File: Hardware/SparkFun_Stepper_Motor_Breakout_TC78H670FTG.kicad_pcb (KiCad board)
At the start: 4 copper layers, 15.2 x 20.3 mm, 45 parts, among them J1 Conn_01x08, J2 Conn_01x08, U1 TC78H670FTG

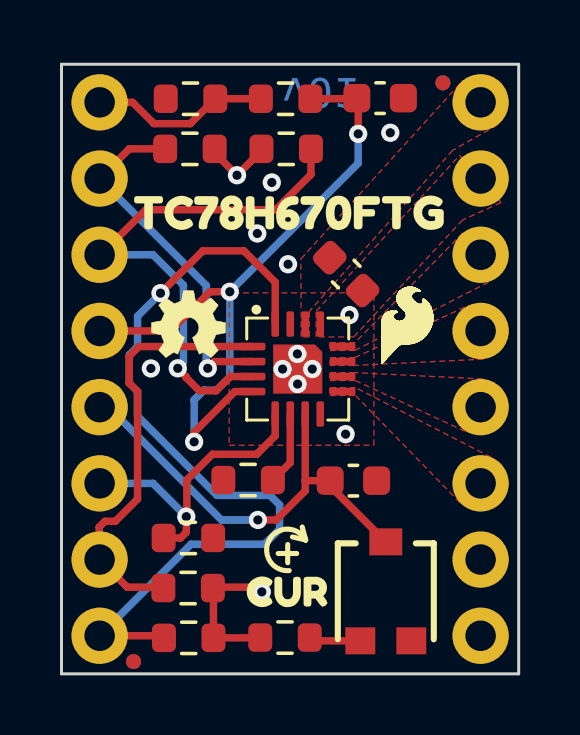
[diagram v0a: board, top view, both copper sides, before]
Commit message: moved fiducials inward
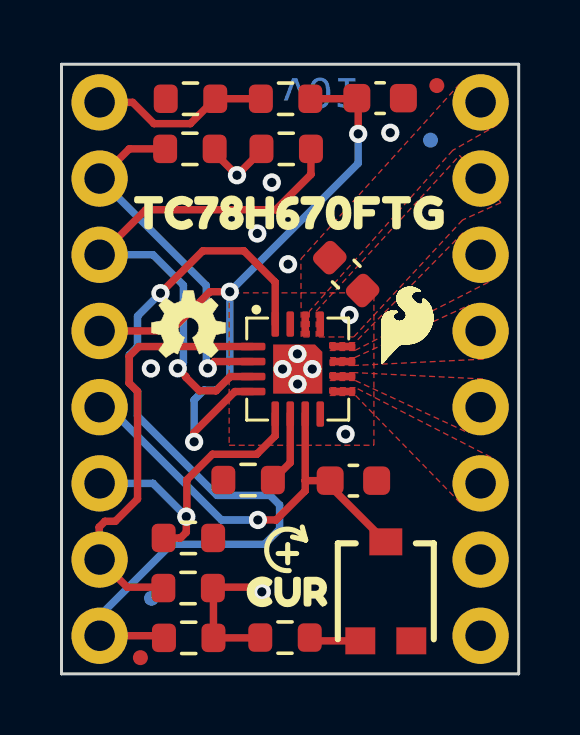
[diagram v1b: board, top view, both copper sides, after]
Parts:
- moved FID3 2.19 mm to (137.6, 111.8)
- moved FID2 1.95 mm to (146.9, 96.5)
- moved FID4 0.26 mm to (137.2, 113.8)
- moved FID1 0.22 mm to (147.1, 94.7)
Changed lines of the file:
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@@
   )
   (footprint "SparkFun-Aesthetic:Fiducial_0.5mm_Mask1mm" (layer "F.Cu")
-    (at 137.021639 113.891825)
+    (at 137.25 113.76)
     (descr "Circular Fiducial, 0.5mm bare copper, 1mm soldermask opening (Level C)")
     (tags "fiducial")
@@
   )
   (footprint "SparkFun-Aesthetic:Fiducial_0.5mm_Mask1mm" (layer "F.Cu")
-    (at 147.331908 94.601097)
+    (at 147.13 94.69)
     (descr "Circular Fiducial, 0.5mm bare copper, 1mm soldermask opening (Level C)")
     (tags "fiducial")
@@
   )
   (footprint "SparkFun-Aesthetic:Fiducial_0.5mm_Mask1mm" (layer "B.Cu")
-    (at 147.331908 94.599043 180)
+    (at 146.92 96.51 180)
     (descr "Circular Fiducial, 0.5mm bare copper, 1mm soldermask opening (Level C)")
     (tags "fiducial")
@@
   )
   (footprint "SparkFun-Aesthetic:Fiducial_0.5mm_Mask1mm" (layer "B.Cu")
-    (at 137.019585 113.89097 180)
+    (at 137.62 111.78 180)
     (descr "Circular Fiducial, 0.5mm bare copper, 1mm soldermask opening (Level C)")
     (tags "fiducial")
@@
     (pts (xy 135.89 114.3) (xy 135.89 113.03))
     (height -5.08)
-    (gr_text "0.05 in" (at 131.953695 112.297205) (layer "Eco1.User")
+    (gr_text "1.27 mm" (at 131.953695 112.297205) (layer "Eco1.User")
       (effects (font (size 0.762 0.762) (thickness 0.15)))
     )
@@
     (pts (xy 134.62 114.3) (xy 134.62 93.98))
     (height -11.43)
-    (gr_text "0.80 in" (at 122.278 104.14 90) (layer "Eco1.User")
+    (gr_text "20.32 mm" (at 122.278 104.14 90) (layer "Eco1.User")
       (effects (font (size 0.762 0.762) (thickness 0.15)))
     )
@@
     (pts (xy 134.62 93.98) (xy 149.86 93.98))
     (height -11.43)
-    (gr_text "0.60 in" (at 142.24 81.638) (layer "Eco1.User")
+    (gr_text "15.24 mm" (at 142.24 81.638) (layer "Eco1.User")
       (effects (font (size 0.762 0.762) (thickness 0.15)))
     )
@@
     (pts (xy 135.89 114.3) (xy 135.89 110.49))
     (height -8.89)
-    (gr_text "0.15 in" (at 125.582655 111.76 90) (layer "Eco1.User")
+    (gr_text "3.81 mm" (at 125.582655 111.76 90) (layer "Eco1.User")
       (effects (font (size 0.762 0.762) (thickness 0.15)))
     )
@@
     (pts (xy 134.62 95.25) (xy 148.59 95.25))
     (height -8.89)
-    (gr_text "0.55 in" (at 141.605 85.448) (layer "Eco1.User")
+    (gr_text "13.97 mm" (at 141.605 85.448) (layer "Eco1.User")
       (effects (font (size 0.762 0.762) (thickness 0.15)))
     )
@@
     (pts (xy 134.62 95.25) (xy 135.89 95.25))
     (height -5.08)
-    (gr_text "0.05 in" (at 137.01647 88.792448) (layer "Eco1.User")
+    (gr_text "1.27 mm" (at 137.01647 88.792448) (layer "Eco1.User")
       (effects (font (size 0.762 0.762) (thickness 0.15)))
     )
@@
     (height 6.56)
     (orientation 0)
-    (gr_text "0.426 in" (at 140.025 117.198) (layer "Eco1.User")
+    (gr_text "10.810 mm" (at 140.025 117.198) (layer "Eco1.User")
       (effects (font (size 0.762 0.762) (thickness 0.15)))
     )
@@
     (height 8.24)
     (orientation 1)
-    (gr_text "0.108 in" (at 153.837301 110.772841) (layer "Eco1.User")
+    (gr_text "2.750 mm" (at 153.837301 110.772841) (layer "Eco1.User")
       (effects (font (size 0.762 0.762) (thickness 0.15)))
     )
@@
   (segment (start 135.89 113.03) (end 137.965 113.03) (width 0.25) (layer "F.Cu") (net 1))
   (via (at 137.92 101.61) (size 0.6096) (drill 0.3048) (layers "F.Cu" "B.Cu") (net 1))
-  (segment (start 137.1548 104.886102) (end 137.1548 105.7048) (width 0.25) (layer "B.Cu") (net 1))
-  (segment (start 138.94 109.98) (end 135.89 113.03) (width 0.25) (layer "B.Cu") (net 1))
-  (segment (start 141.57 108.35) (end 141.89 108.67) (width 0.25) (layer "B.Cu") (net 1))
   (segment (start 141.89 108.67) (end 141.89 109.48) (width 0.25) (layer "B.Cu") (net 1))
-  (segment (start 137.1548 103.393898) (end 136.88 103.668698) (width 0.25) (layer "B.Cu") (net 1))
-  (segment (start 137.1548 102.3752) (end 137.1548 103.393898) (width 0.25) (layer "B.Cu") (net 1))
+  (segment (start 141.57 108.35) (end 141.89 108.67) (width 0.25) (layer "B.Cu") (net 1))
+  (segment (start 138.28 109.98) (end 135.89 112.37) (width 0.25) (layer "B.Cu") (net 1))
+  (segment (start 135.89 112.37) (end 135.89 113.03) (width 0.25) (layer "B.Cu") (net 1))
   (segment (start 137.1548 105.7048) (end 139.8 108.35) (width 0.25) (layer "B.Cu") (net 1))
-  (segment (start 137.92 101.61) (end 137.1548 102.3752) (width 0.25) (layer "B.Cu") (net 1))
-  (segment (start 141.89 109.48) (end 141.39 109.98) (width 0.25) (layer "B.Cu") (net 1))
   (segment (start 136.88 104.611302) (end 137.1548 104.886102) (width 0.25) (layer "B.Cu") (net 1))
-  (segment (start 141.39 109.98) (end 138.94 109.98) (width 0.25) (layer "B.Cu") (net 1))
+  (segment (start 141.39 109.98) (end 138.28 109.98) (width 0.25) (layer "B.Cu") (net 1))
   (segment (start 139.8 108.35) (end 141.57 108.35) (width 0.25) (layer "B.Cu") (net 1))
+  (segment (start 137.1548 103.393898) (end 136.88 103.668698) (width 0.25) (layer "B.Cu") (net 1))
+  (segment (start 137.1548 104.886102) (end 137.1548 105.7048) (width 0.25) (layer "B.Cu") (net 1))
+  (segment (start 137.92 101.61) (end 137.1548 102.3752) (width 0.25) (layer "B.Cu") (net 1))
+  (segment (start 137.1548 102.3752) (end 137.1548 103.393898) (width 0.25) (layer "B.Cu") (net 1))
   (segment (start 136.88 103.668698) (end 136.88 104.611302) (width 0.25) (layer "B.Cu") (net 1))
+  (segment (start 141.89 109.48) (end 141.39 109.98) (width 0.25) (layer "B.Cu") (net 1))
   (segment (start 142.935 96.8) (end 142.935 97.655) (width 0.25) (layer "F.Cu") (net 2))
   (segment (start 141.76 98.83) (end 137.43 98.83) (width 0.25) (layer "F.Cu") (net 2))

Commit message: updated trimpot
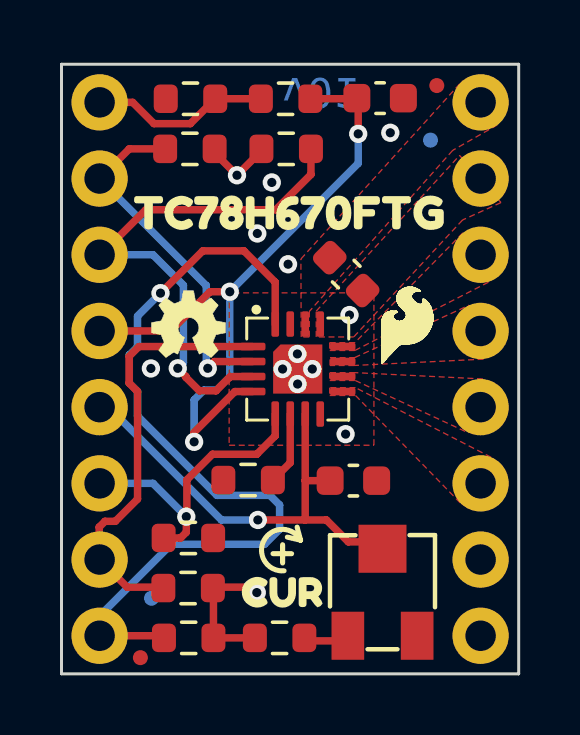
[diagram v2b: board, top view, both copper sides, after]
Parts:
- removed G1: OSHW_Logo, SparkFun-Aesthetic:Creative_Commons_License
- RV1: footprint SparkFun-Resistor:TRIMPOT-SMD-3MM-CLOSED -> SparkFun-Resistor:Trimpot_SMD_3.0x3.0mm
- moved R1 0.18 mm to (141.9, 113.1)
- moved kibuzzard-65D531EE 0.16 mm to (142.0, 111.6)
- moved RV1 0.11 mm to (145.3, 111.6)
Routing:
- net VREF: track 15.0 -> 15.8 mm

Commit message: corrected motor driver IC footprint
I had the pins numbered incorrectly, had to re-route most things.
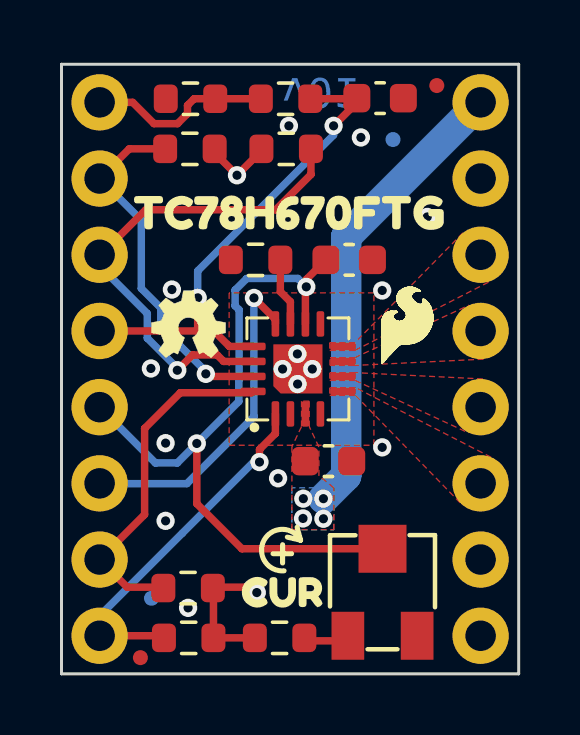
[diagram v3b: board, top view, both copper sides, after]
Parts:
- removed the R8 at (138.8, 109.8)
- added G2: OSHW_Logo, SparkFun-Aesthetic:Creative_Commons_License, F.Cu at (0.25, 0.25)
- moved kibuzzard-65CFAB85 7.62 mm to (146.3, 100.3)
- moved kibuzzard-65CFAE3D 7.62 mm to (146.2, 108.0)
- moved C2 7.36 mm to (144.2, 100.5)
- moved R10 7.34 mm to (141.1, 100.5)
- moved C1 6.26 mm to (143.5, 107.2), turned to 0 degrees
- moved U1 3.35 mm to (143.2, 105.6), turned to 180 degrees
- moved kibuzzard-65CFAB77 2.54 mm to (146.4, 102.9)
- moved kibuzzard-65CFAB5A 2.53 mm to (146.3, 105.4)
- moved FID3 1.25 mm to (145.7, 96.5)
- renumbered C2 to C1, C1 to C2, FID3 to FID2, FID2 to FID3, R3 to R10, R9 to R3, R2 to R4, R4 to R5, R5 to R7, R6 to R8, R7 to R9
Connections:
- J2 pad 3: A+ -> B+
- J2 pad 4: A- -> B-
- J2 pad 5: B- -> A-
- J2 pad 6: B+ -> A+
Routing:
- net DIR: track 27.7 -> 12.1 mm
- net VM: track 0.00 -> 15.4 mm, vias 0 -> 4
- net VREF: track 15.8 -> 23.9 mm, vias 1 -> 2
- net ERR: track 23.3 -> 16.8 mm, vias 3 -> 2
- net STEP: track 14.4 -> 11.6 mm
- net MODE0: track 18.1 -> 16.8 mm
- net ~{STBY}: track 10.2 -> 11.2 mm
- net GND: vias 11 -> 15
- added copper zone on B.Cu, net VM

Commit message: checklist stuff
-added 1,2,3,4 to copper layers
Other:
- board text added: "1"
- board text added: "2"
- board text added: "3"
- board text added: "4"
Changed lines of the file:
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@@
   (gr_rect (start 134.62 93.98) (end 149.86 114.3)
     (stroke (width 0.1) (type default)) (fill none) (layer "Edge.Cuts"))
+  (gr_text "1" (at 143.65 111.22) (layer "F.Cu")
+    (effects (font (size 0.5 0.5) (thickness 0.1) bold) (justify left bottom))
+  )
+  (gr_text "2" (at 143.65 111.22) (layer "In1.Cu")
+    (effects (font (size 0.5 0.5) (thickness 0.1) bold) (justify left bottom))
+  )
+  (gr_text "3" (at 143.66 111.22) (layer "In2.Cu")
+    (effects (font (size 0.5 0.5) (thickness 0.1) bold) (justify left bottom))
+  )
   (gr_text "v01" (at 141.988553 94.318209 180) (layer "B.Cu")
     (effects (font (size 1 1) (thickness 0.15)) (justify left bottom mirror))
+  )
+  (gr_text "4" (at 144.2 111.22) (layer "B.Cu")
+    (effects (font (size 0.5 0.5) (thickness 0.1) bold) (justify left bottom mirror))
   )
   (gr_text "Solder Mask: Red" (at 170.27 70.77) (layer "F.Fab")
@@
     (pts (xy 135.89 114.3) (xy 135.89 113.03))
     (height -5.08)
-    (gr_text "0.05 in" (at 131.953695 112.297205) (layer "Eco1.User")
+    (gr_text "1.27 mm" (at 131.953695 112.297205) (layer "Eco1.User")
       (effects (font (size 0.762 0.762) (thickness 0.15)))
     )
@@
     (pts (xy 134.62 114.3) (xy 134.62 93.98))
     (height -11.43)
-    (gr_text "0.80 in" (at 122.278 104.14 90) (layer "Eco1.User")
+    (gr_text "20.32 mm" (at 122.278 104.14 90) (layer "Eco1.User")
       (effects (font (size 0.762 0.762) (thickness 0.15)))
     )
@@
     (pts (xy 134.62 93.98) (xy 149.86 93.98))
     (height -11.43)
-    (gr_text "0.60 in" (at 142.24 81.638) (layer "Eco1.User")
+    (gr_text "15.24 mm" (at 142.24 81.638) (layer "Eco1.User")
       (effects (font (size 0.762 0.762) (thickness 0.15)))
     )
@@
     (pts (xy 135.89 114.3) (xy 135.89 110.49))
     (height -8.89)
-    (gr_text "0.15 in" (at 125.582655 111.76 90) (layer "Eco1.User")
+    (gr_text "3.81 mm" (at 125.582655 111.76 90) (layer "Eco1.User")
       (effects (font (size 0.762 0.762) (thickness 0.15)))
     )
@@
     (pts (xy 134.62 95.25) (xy 148.59 95.25))
     (height -8.89)
-    (gr_text "0.55 in" (at 141.605 85.448) (layer "Eco1.User")
+    (gr_text "13.97 mm" (at 141.605 85.448) (layer "Eco1.User")
       (effects (font (size 0.762 0.762) (thickness 0.15)))
     )
@@
     (pts (xy 134.62 95.25) (xy 135.89 95.25))
     (height -5.08)
-    (gr_text "0.05 in" (at 137.01647 88.792448) (layer "Eco1.User")
+    (gr_text "1.27 mm" (at 137.01647 88.792448) (layer "Eco1.User")
       (effects (font (size 0.762 0.762) (thickness 0.15)))
     )
@@
     (height 6.56)
     (orientation 0)
-    (gr_text "0.426 in" (at 140.025 117.198) (layer "Eco1.User")
+    (gr_text "10.810 mm" (at 140.025 117.198) (layer "Eco1.User")
       (effects (font (size 0.762 0.762) (thickness 0.15)))
     )
@@
     (height 8.24)
     (orientation 1)
-    (gr_text "0.108 in" (at 153.837301 110.772841) (layer "Eco1.User")
+    (gr_text "2.750 mm" (at 153.837301 110.772841) (layer "Eco1.User")
       (effects (font (size 0.762 0.762) (thickness 0.15)))
     )
@@
     (style (thickness 0.15) (arrow_length 0.508) (text_position_mode 2) (extension_height 0.58642) (extension_offset 0.5))
   )
-  (segment (start 141.22 106.82) (end 141.75 106.29) (width 0.25) (layer "F.Cu") (net 1))
-  (segment (start 141.22 107.24) (end 141.22 106.82) (width 0.25) (layer "F.Cu") (net 1))
+  (segment (start 141.22 107.24) (end 141.22 106.75) (width 0.25) (layer "F.Cu") (net 1))
+  (segment (start 141.75 106.22) (end 141.75 105.636025) (width 0.25) (layer "F.Cu") (net 1))
   (segment (start 137.965 113.03) (end 138.035 113.1) (width 0.25) (layer "F.Cu") (net 1))
-  (segment (start 141.75 106.29) (end 141.75 105.636025) (width 0.25) (layer "F.Cu") (net 1))
+  (segment (start 141.22 106.75) (end 141.75 106.22) (width 0.25) (layer "F.Cu") (net 1))
   (segment (start 135.89 113.03) (end 137.965 113.03) (width 0.25) (layer "F.Cu") (net 1))
   (via (at 141.22 107.24) (size 0.6096) (drill 0.3048) (layers "F.Cu" "B.Cu") (net 1))
@@
   (segment (start 135.89 105.41) (end 137.75 107.27) (width 0.25) (layer "B.Cu") (net 6))
   (segment (start 140.53 105.22) (end 140.53 104.48) (width 0.25) (layer "B.Cu") (net 6))
-  (segment (start 141.75 102.636025) (end 141.75 102.485) (width 0.25) (layer "F.Cu") (net 7))
-  (segment (start 141.75 102.485) (end 141.035153 101.770153) (width 0.25) (layer "F.Cu") (net 7))
+  (segment (start 141.75 102.031701) (end 141.488452 101.770153) (width 0.25) (layer "F.Cu") (net 7))
+  (segment (start 141.75 102.636025) (end 141.75 102.031701) (width 0.25) (layer "F.Cu") (net 7))
+  (segment (start 141.488452 101.770153) (end 141.035153 101.770153) (width 0.25) (layer "F.Cu") (net 7))
   (via (at 141.035153 101.770153) (size 0.6096) (drill 0.3048) (layers "F.Cu" "B.Cu") (net 7))
   (segment (start 141.035153 105.724847) (end 138.8 107.96) (width 0.25) (layer "B.Cu") (net 7))
